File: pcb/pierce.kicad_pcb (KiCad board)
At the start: 2 copper layers, 227.3 x 105.6 mm, 81 parts, among them J1 Conn_01x10, J2 Conn_01x10, J3 Trackpoint, SW1 SW_PUSH, SW10 SW_PUSH, SW11 SW_PUSH, SW12 SW_PUSH, SW13 SW_PUSH, SW14 SW_PUSH, SW15 SW_PUSH, SW16 SW_PUSH, SW17 SW_PUSH, SW18 SW_PUSH, SW19 SW_PUSH, SW2 SW_PUSH, SW20 SW_PUSH, SW21 SW_PUSH, SW22 SW_PUSH, SW23 SW_PUSH, SW24 SW_PUSH, SW25 SW_PUSH, SW26 SW_PUSH, SW27 SW_PUSH, SW28 SW_PUSH, SW29 SW_PUSH, SW3 SW_PUSH, SW30 SW_PUSH, SW31 SW_PUSH, SW32 SW_PUSH, SW33 SW_PUSH, SW34 SW_PUSH, SW35 SW_PUSH, SW36 SW_PUSH, SW37 SW_PUSH, SW4 SW_PUSH, SW5 SW_PUSH, SW6 SW_PUSH, SW7 SW_PUSH, SW8 SW_PUSH, SW9 SW_PUSH, U1 Elite-C_reverse

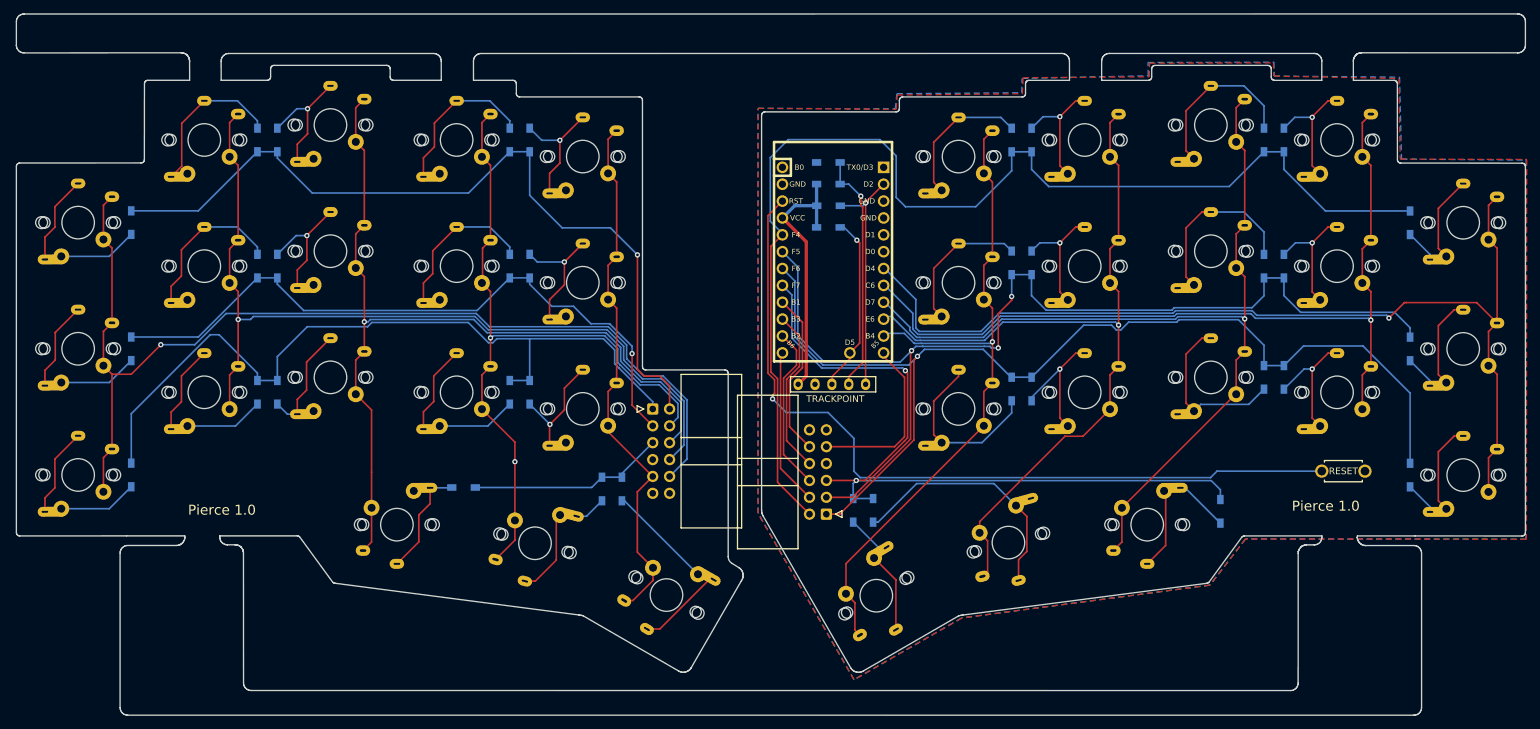
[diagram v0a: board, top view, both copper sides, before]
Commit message: added back missing mounting holes
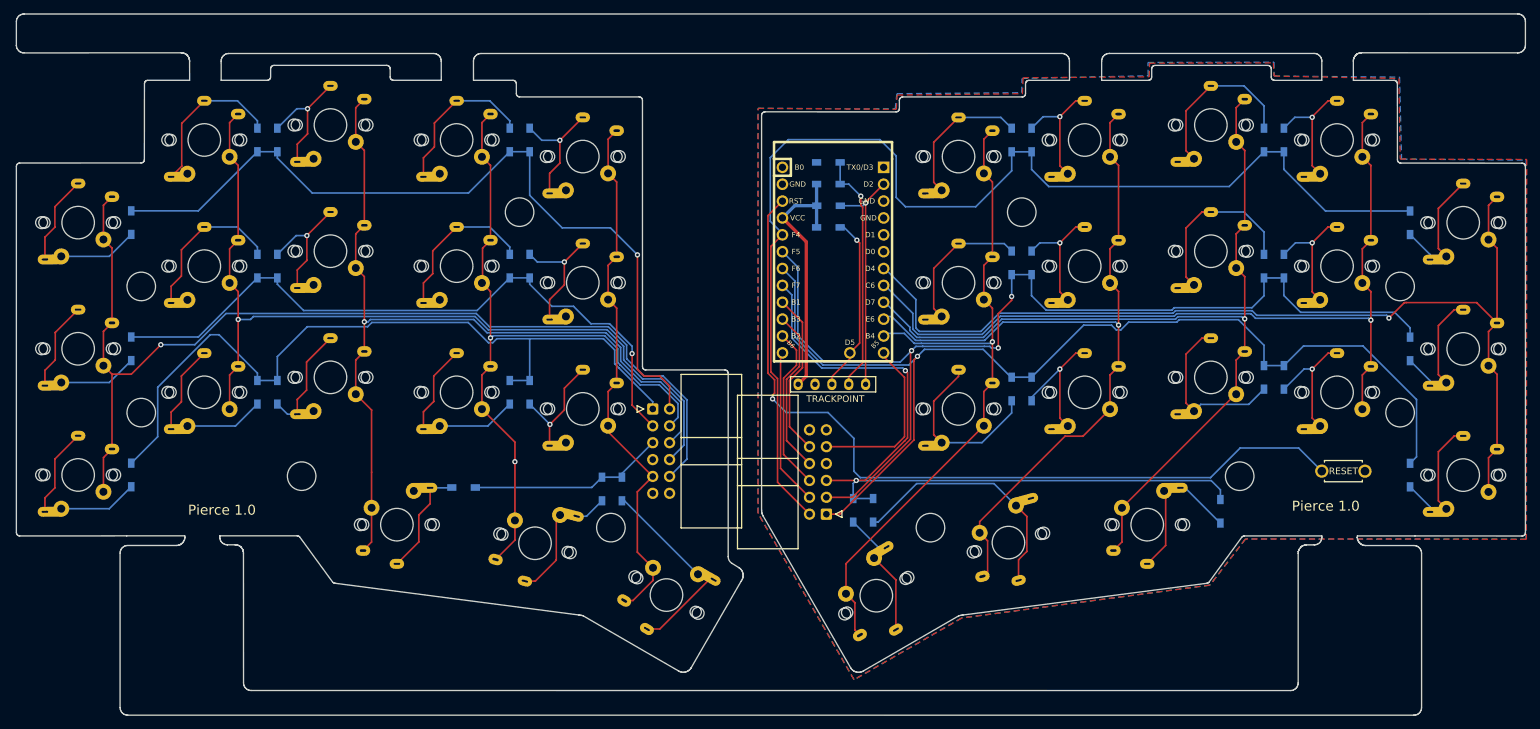
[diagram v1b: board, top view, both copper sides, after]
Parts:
- added Ref**: Val**, kbd:M2_HOLE_v2, F.Cu at (53.7, 57.3)
- added Ref**: Val**, kbd:M2_HOLE_v2, F.Cu at (219.1, 85.8)
- added Ref**: Val**, kbd:M2_HOLE_v2, F.Cu at (53.7, 76.3)
- added Ref**: Val**, kbd:M2_HOLE_v2, F.Cu at (110.6, 46.1)
- added Ref**: Val**, kbd:M2_HOLE_v2, F.Cu at (124.4, 93.6)
- added Ref**: Val**, kbd:M2_HOLE_v2, F.Cu at (77.8, 85.8)
- added Ref**: Val**, kbd:M2_HOLE_v2, F.Cu at (243.3, 57.3)
- added Ref**: Val**, kbd:M2_HOLE_v2, F.Cu at (243.3, 76.3)
- added Ref**: Val**, kbd:M2_HOLE_v2, F.Cu at (186.3, 46.1)
- added Ref**: Val**, kbd:M2_HOLE_v2, F.Cu at (172.5, 93.6)
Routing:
- net reset: track 122.2 -> 125.0 mm
- net row2: track 162.4 -> 163.2 mm

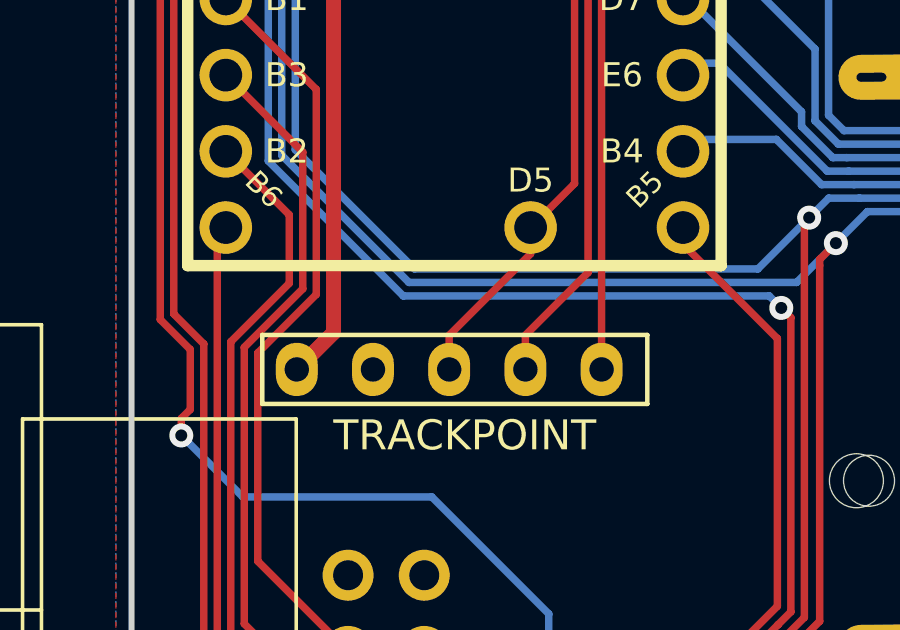
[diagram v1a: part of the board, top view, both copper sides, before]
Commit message: added silk text
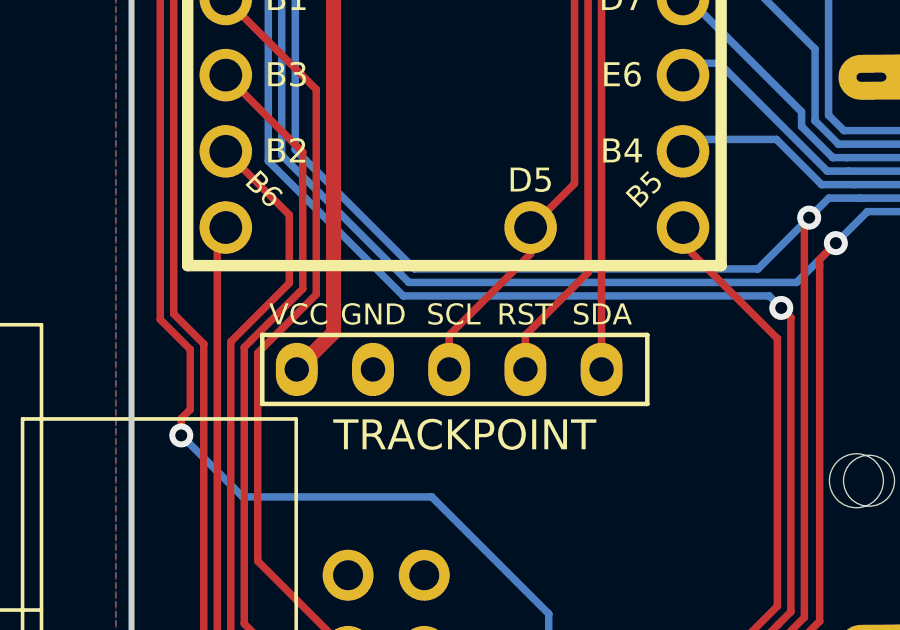
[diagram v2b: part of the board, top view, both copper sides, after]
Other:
- board text added: "GND"
- board text added: "RST"
- board text added: "SCL"
- board text added: "SDA"
- board text added: "VCC"

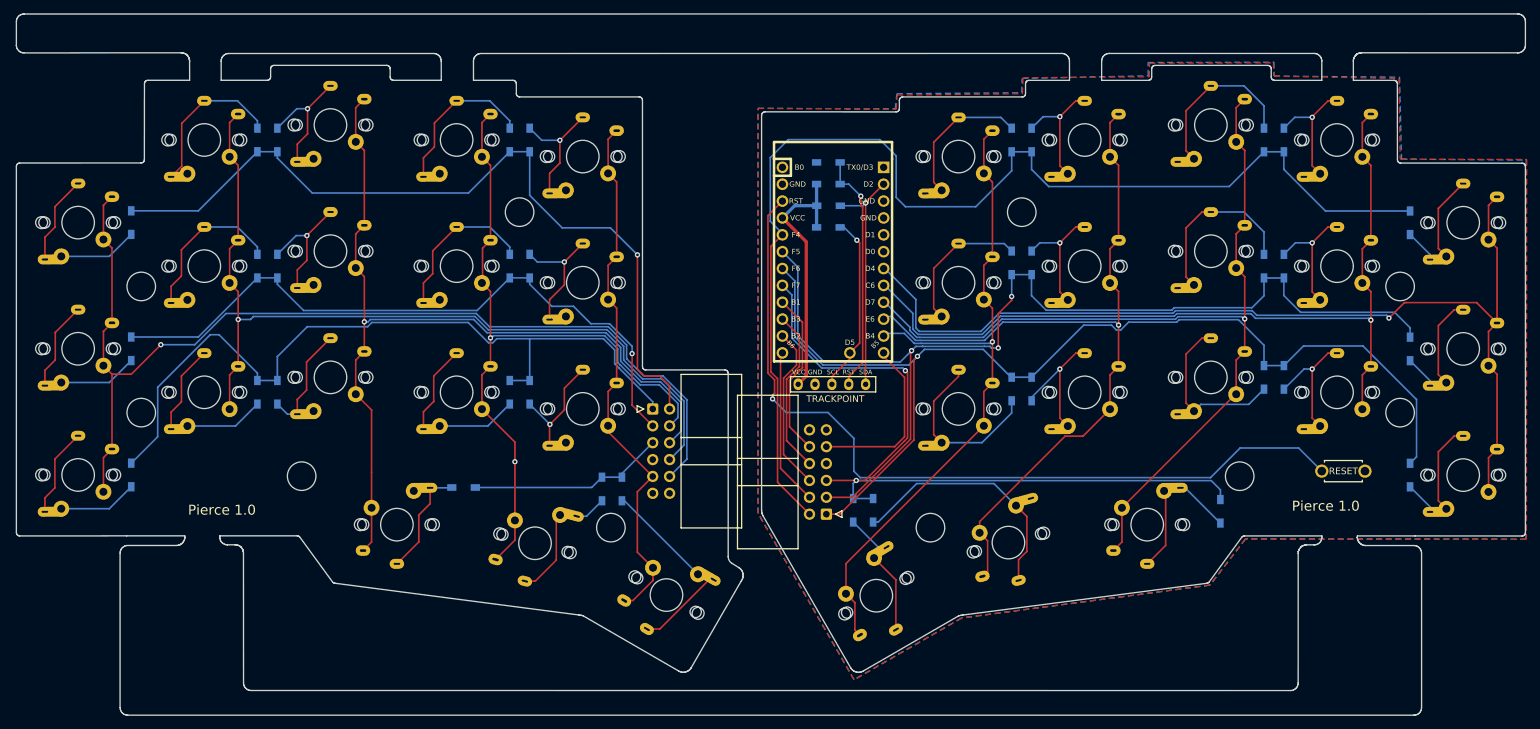
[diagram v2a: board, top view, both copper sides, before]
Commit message: add connection for rotary encoder
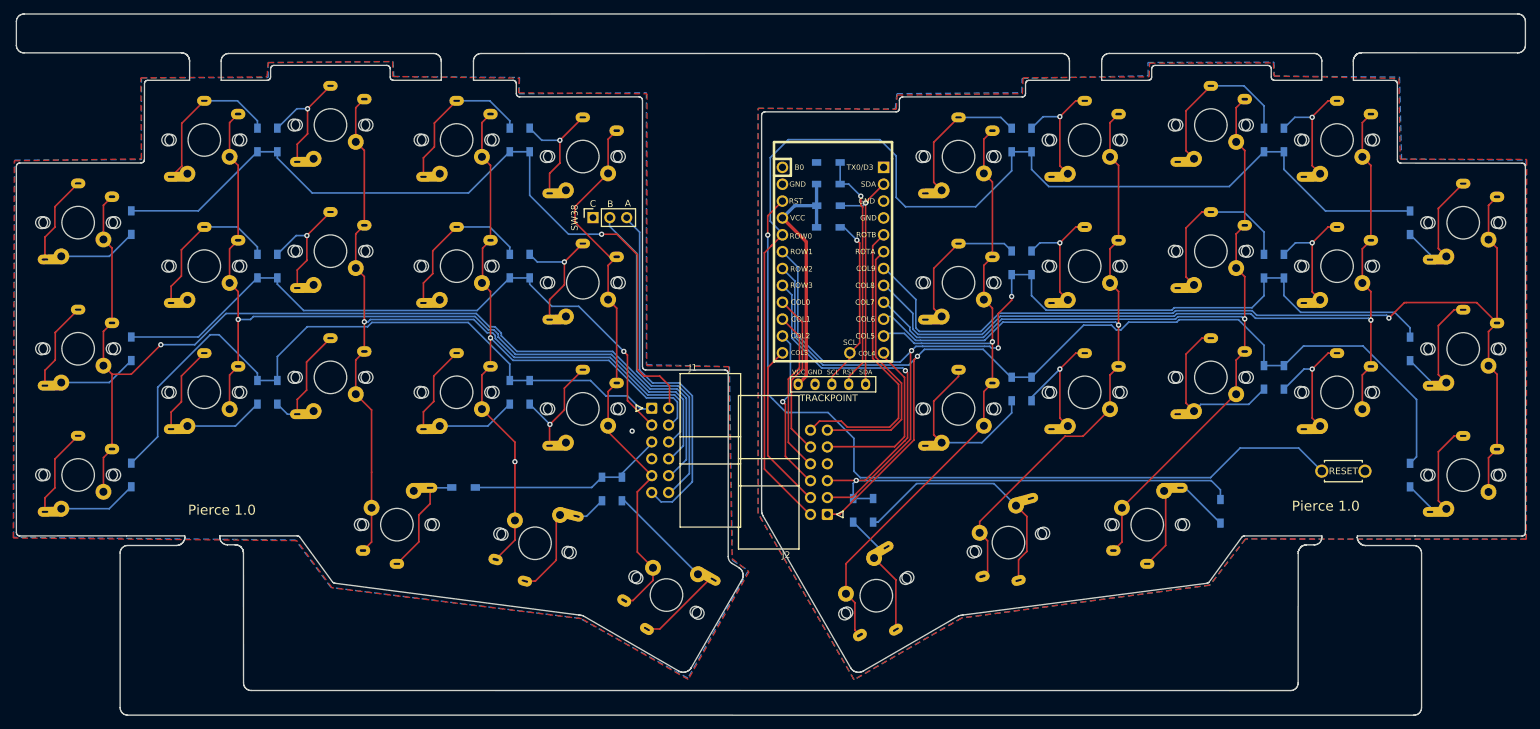
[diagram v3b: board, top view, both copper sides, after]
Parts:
- removed Ref** (x10): Val**, kbd:M2_HOLE_v2
- added SW38: Rotary_Encoder, pierce:Rotary_encoder_conn, F.Cu at (121.7, 46.9)
- J1, J2: value Conn_01x10 -> Conn_01x12
- moved J1 0.19 mm to (130.6, 75.6)
- moved J2 0.16 mm to (157.0, 91.6)
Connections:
- J1 pad 11: (no net) -> rotal
- J1 pad 12: (no net) -> rotbl
- J1 pad 7: (no net) -> GND1
- J2 pad 11: (no net) -> rota
- J2 pad 12: (no net) -> rotb
- J2 pad 7: (no net) -> GND
- U1 pad 5: (no net) -> rotb
- U1 pad 6: (no net) -> rota
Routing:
- net rotal: track 0.00 -> 54.0 mm
- net rotbl: track 0.00 -> 49.9 mm
- net rotb: track 0.00 -> 44.7 mm
- net rota: track 0.00 -> 39.2 mm
- net row2l: track 117.2 -> 107.0 mm
- net col4l: track 80.7 -> 85.5 mm
- net col3: track 23.7 -> 25.7 mm
- net col3l: track 110.7 -> 109.3 mm
- net row1l: track 101.8 -> 100.6 mm
- net row0: track 178.7 -> 179.7 mm
- net col0l: track 156.7 -> 155.7 mm
- net col2l: track 133.2 -> 132.2 mm
- net col1l: track 130.6 -> 129.7 mm
- net col2: track 25.1 -> 24.4 mm, vias 0 -> 1
- net GND1: vias 0 -> 1
- added copper zone on B.Cu, net GND1
- added copper zone on F.Cu, net GND1
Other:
- board text added: "A"
- board text added: "B"
- board text added: "C"
- board text added: "COL0"
- board text added: "COL1"
- board text added: "COL2"
- board text added: "COL3"
- board text added: "COL4"
- board text added: "COL5"
- board text added: "COL6"
- board text added: "COL7"
- board text added: "COL8"
- board text added: "ROW0"
- board text added: "ROW1"
- board text added: "ROW2"
- board text added: "ROW3"
